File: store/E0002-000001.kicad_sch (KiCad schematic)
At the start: 19 parts, among them J6 Seansor_Header_A, J7 Seansor_Header_B, U1 SHT45-AD1F-R2, U2 BME688, U3 SCD41-D-R2, U4 TLV70018_SOT353, U5 NCP114AMX280TCG

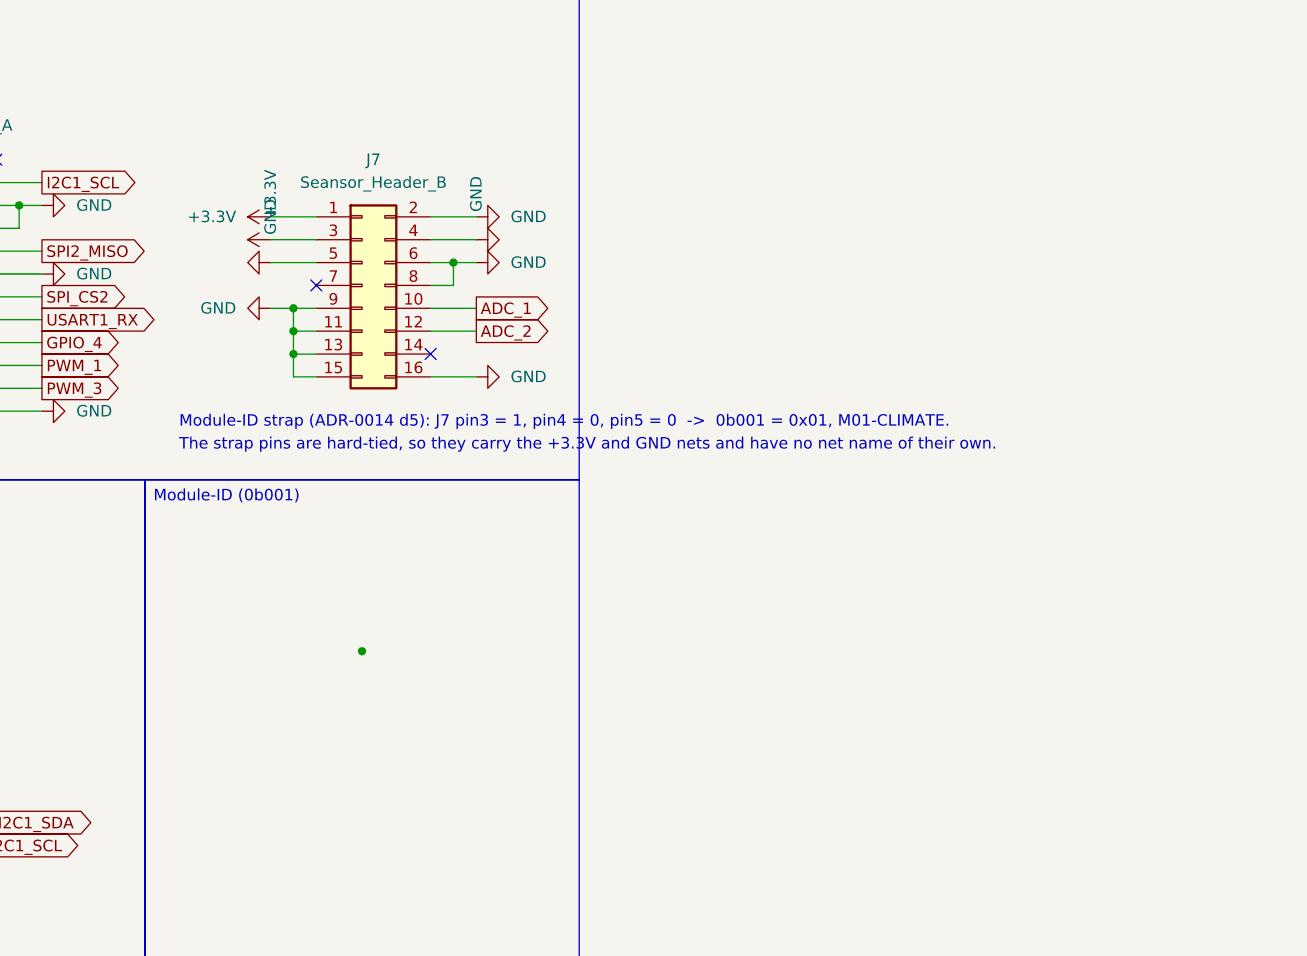
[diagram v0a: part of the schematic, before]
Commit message: Revert "M01: name the E0002 power nets GND and +3.3V"
This reverts f28e02d. The STRAP_x labels are back on the schematic and the
PCB nets are STRAP_1 and STRAP_0 again, at the same 168 and 70 references.

Also stores the DRC exclusion in the [key, comment] form KiCad itself
writes, replacing the bare string.

Signed-off-by: IIchukissII <133657307+IIchukissII@users.noreply.github.com>
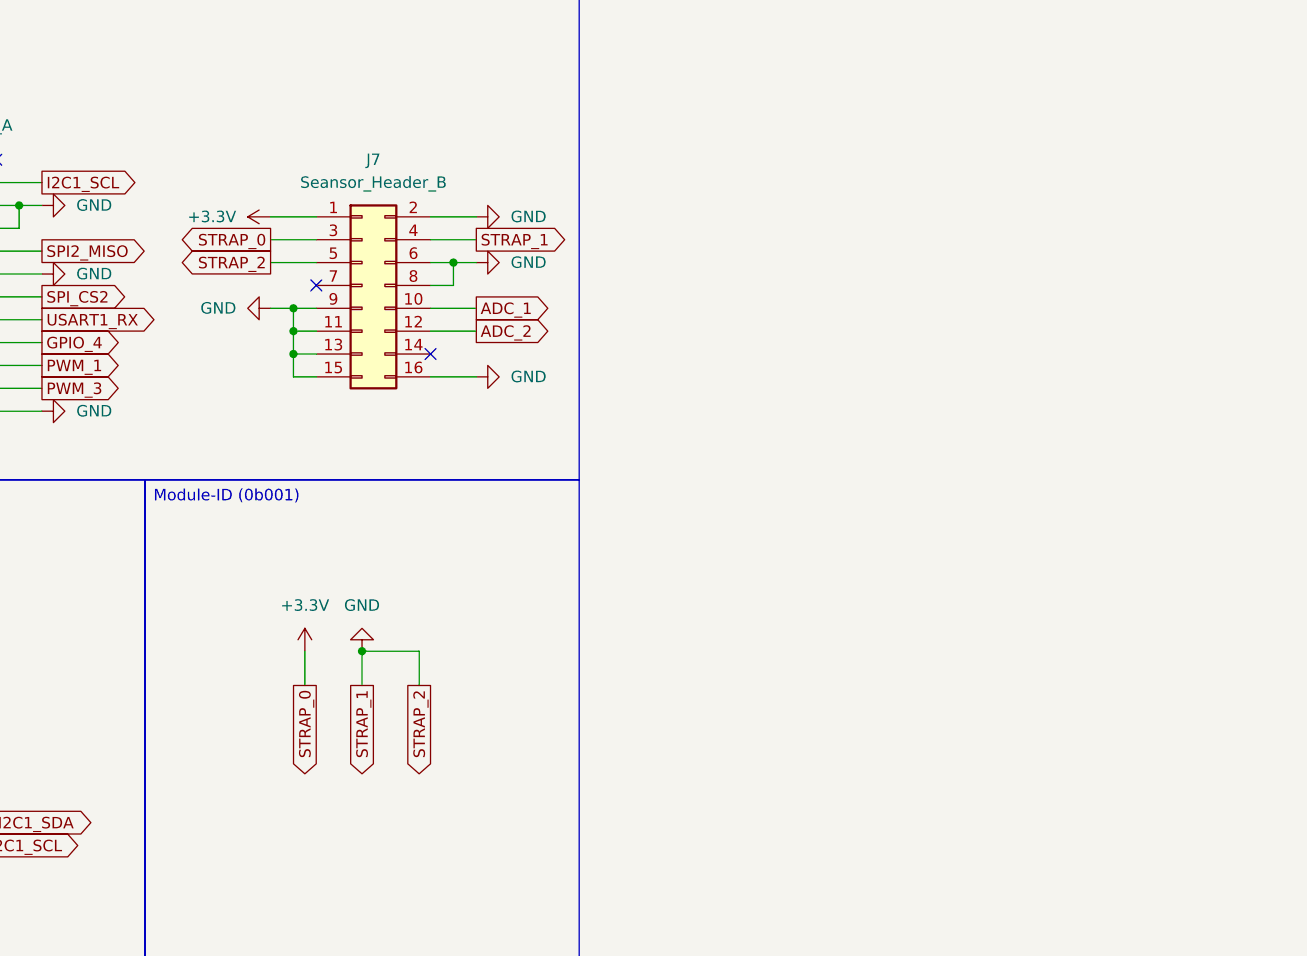
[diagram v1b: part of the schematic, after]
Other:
- note removed: "Module-ID strap (ADR-0014 d5): J7 pin3 = 1, pin4 = 0, pin5 = 0 -> 0b001 = 0x01, M01-CLIMATE."
- note removed: "The strap pins are hard-tied, so they carry the +3.3V and GND nets and have no net name of their own."

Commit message: M01: name the E0002 power nets GND and +3.3V
The straps are hard-tied to the rails (ADR-0014 d5), and the STRAP_x
global labels outranked the power symbols: the ground plane was named
STRAP_1, the 3V3 rail STRAP_0, and no GND net existed. The labels and
the tie block are removed; J7 pins 3, 4 and 5 tie to +3.3V, GND and GND
directly, with the strap pattern kept as schematic text.

Connectivity unchanged: 93 of 93 pad-to-net assignments identical under
the rename. ERC 21 -> 19, losing the two multiple_net_names warnings.
PCB nets renamed to match; DRC unchanged, parity clean.

Signed-off-by: IIchukissII <133657307+IIchukissII@users.noreply.github.com>
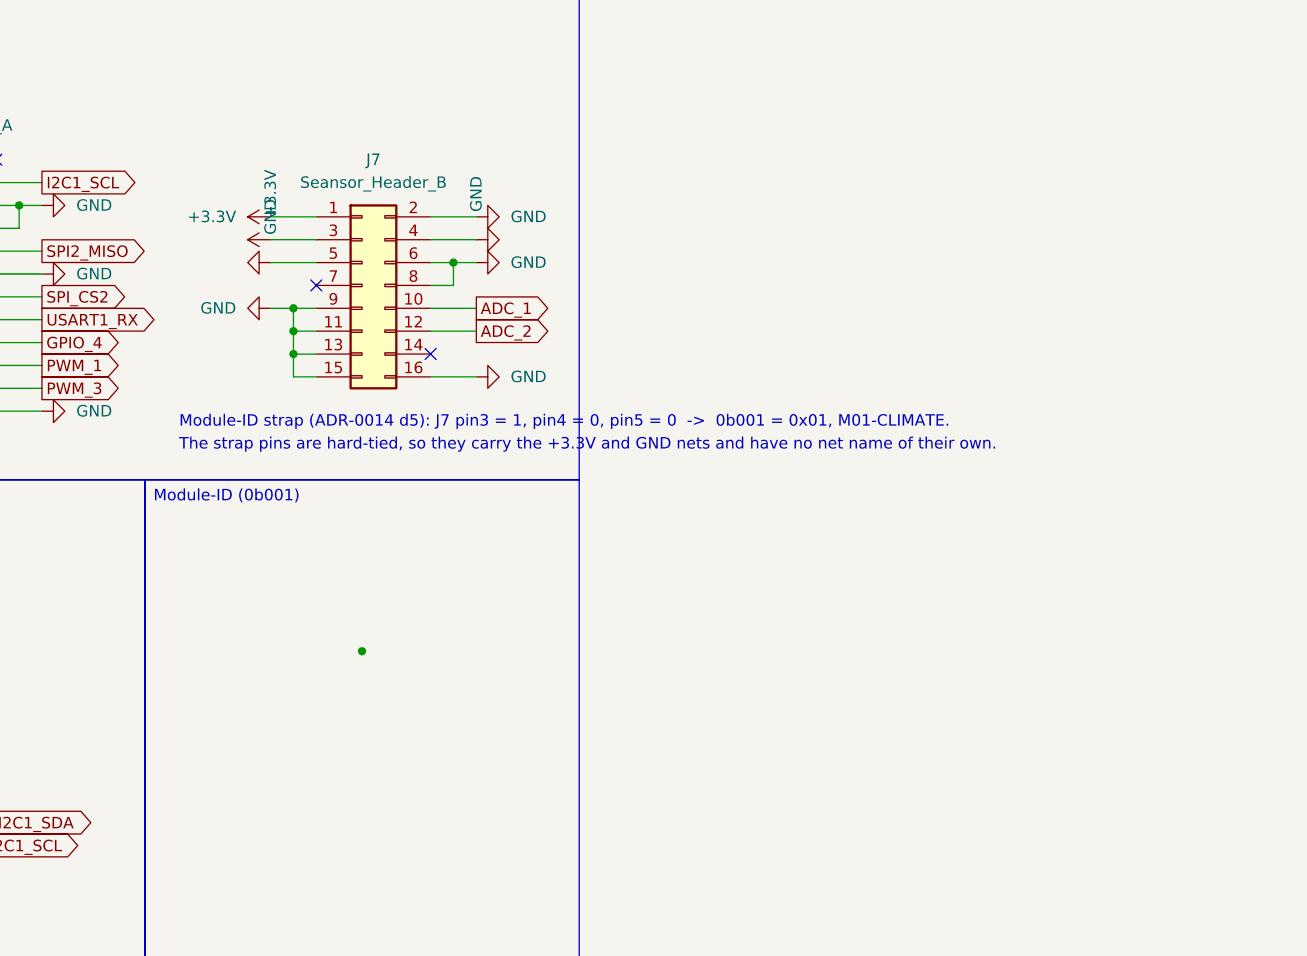
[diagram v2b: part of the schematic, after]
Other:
- note added: "Module-ID strap (ADR-0014 d5): J7 pin3 = 1, pin4 = 0, pin5 = 0 -> 0b001 = 0x01, M01-CLIMATE."
- note added: "The strap pins are hard-tied, so they carry the +3.3V and GND nets and have no net name of their own."
